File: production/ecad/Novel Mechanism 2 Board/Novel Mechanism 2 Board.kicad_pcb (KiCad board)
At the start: 2 copper layers, 37.4 x 45 mm, 19 parts, among them J1 1755736, J2 1755736, J3 0532611271, U1 L9958SBTR, U2 TMCS1108A4BQDRQ1

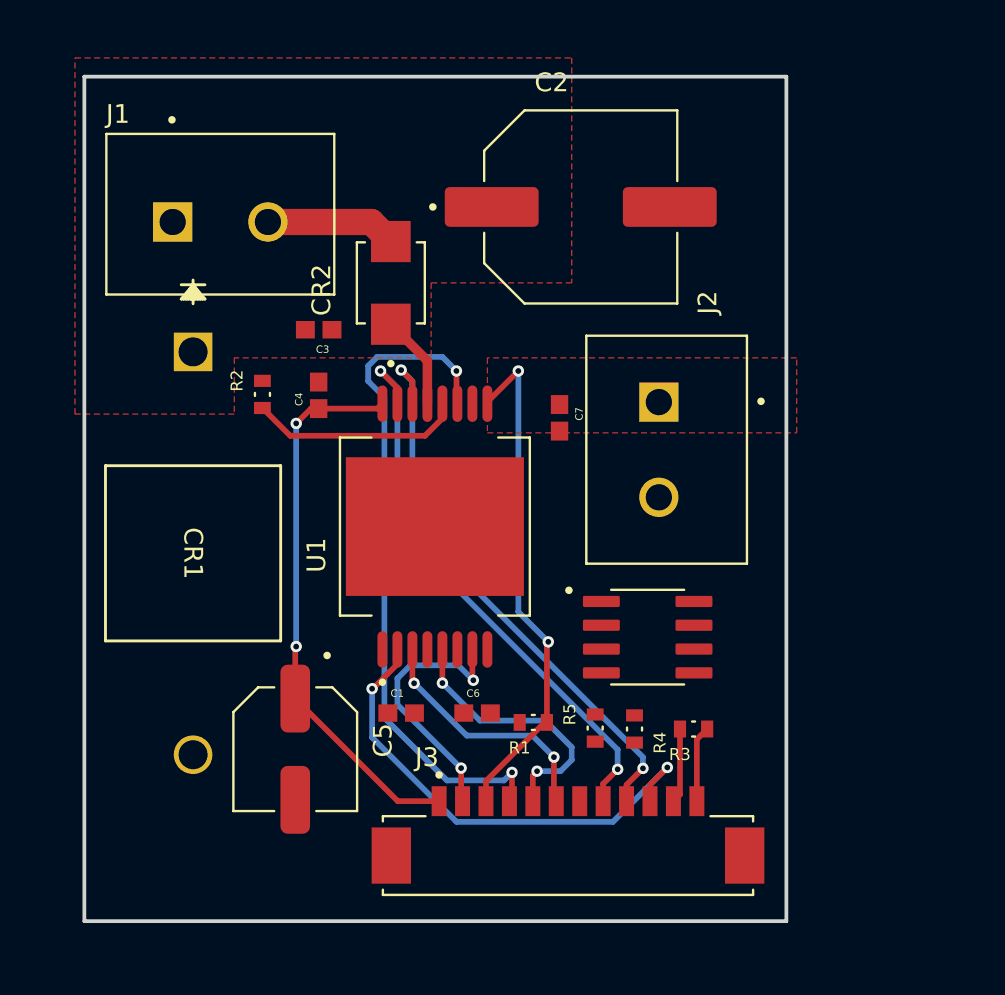
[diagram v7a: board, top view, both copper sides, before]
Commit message: routing complete - preteardrops
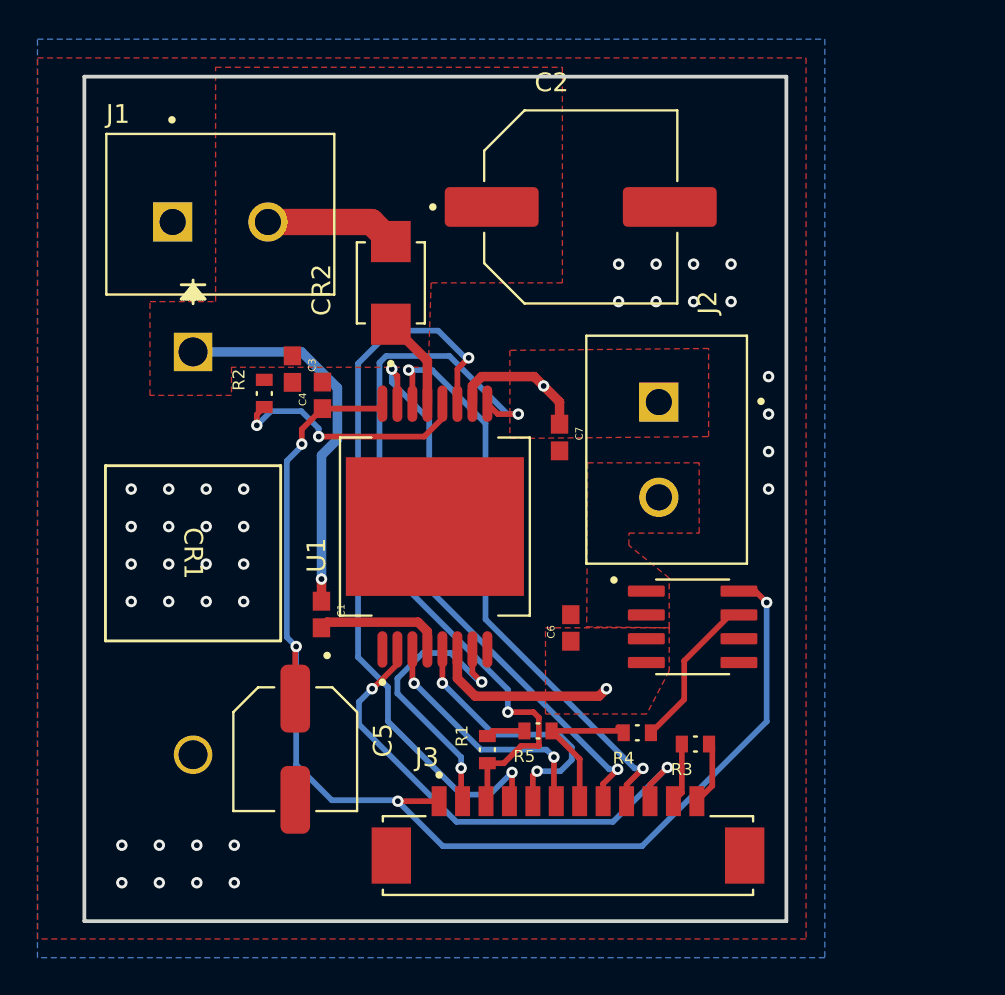
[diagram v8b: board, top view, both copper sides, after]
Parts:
- moved C1 6.76 mm to (131.2, 74.7), turned to -90 degrees
- moved C6 6.75 mm to (144.4, 75.4), turned to 90 degrees
- moved R5 3.05 mm to (142.7, 80.9), turned to 180 degrees
- moved R1 2.85 mm to (140.0, 81.9), turned to 90 degrees
- moved C3 2.52 mm to (129.6, 61.6), turned to -90 degrees
- moved U2 2.46 mm to (150.9, 75.3)
- moved C7 1.05 mm to (143.8, 65.2)
- moved R3 0.81 mm to (151.1, 81.6)
- moved R4 0.25 mm to (148.0, 81.0), turned to 180 degrees
- moved C4 0.20 mm to (131.2, 63.0)
- moved R2 0.11 mm to (128.1, 62.9)
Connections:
- J2 pad 2: Net-(U2-IN-) -> Net-(U2-IN+)
- U2 pad 1: Net-(U1-OUT1) -> Net-(U2-IN+)
- U2 pad 2: Net-(U1-OUT1) -> Net-(U2-IN+)
- U2 pad 3: Net-(U2-IN-) -> Net-(U1-OUT1)
- U2 pad 4: Net-(U2-IN-) -> Net-(U1-OUT1)
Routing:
- net +5V: track 29.7 -> 66.0 mm, vias 2 -> 4
- net +15V: track 5.05 -> 25.3 mm, vias 0 -> 1
- net /Enable: track 27.5 -> 40.7 mm
- net Net-(U1-OUT1): track 0.00 -> 10.1 mm, vias 0 -> 1
- net /AOUT: track 0.00 -> 8.69 mm
- net Net-(U2-VOUT): track 0.00 -> 8.51 mm
- net Net-(U1-OUT2): track 0.00 -> 7.31 mm, vias 0 -> 1
- net Net-(U1-CP): track 0.00 -> 6.94 mm
- net /PWM: track 36.1 -> 40.0 mm
- net GND: track 0.00 -> 2.09 mm, vias 0 -> 36
- net Net-(U1-REXT): track 12.2 -> 14.2 mm, vias 0 -> 2
- net /Disable: track 14.3 -> 15.6 mm
- net /DET: track 4.02 -> 3.26 mm
- net /SI: track 30.7 -> 31.4 mm
- net Net-(J3-Pad12): track 4.08 -> 3.46 mm
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- added copper zone on B.Cu, net GND
- added copper zone on F.Cu, net GND
- added copper zone on F.Cu, net Net-(U1-OUT1)
- added copper zone on F.Cu, net Net-(U2-IN+)
